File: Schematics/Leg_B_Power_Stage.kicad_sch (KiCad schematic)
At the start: 38 parts, among them Q4 C3M0025065K, Q5 C3M0025065K, U3 UCC21710QDWRQ1, U4 UCC21710QDWRQ1

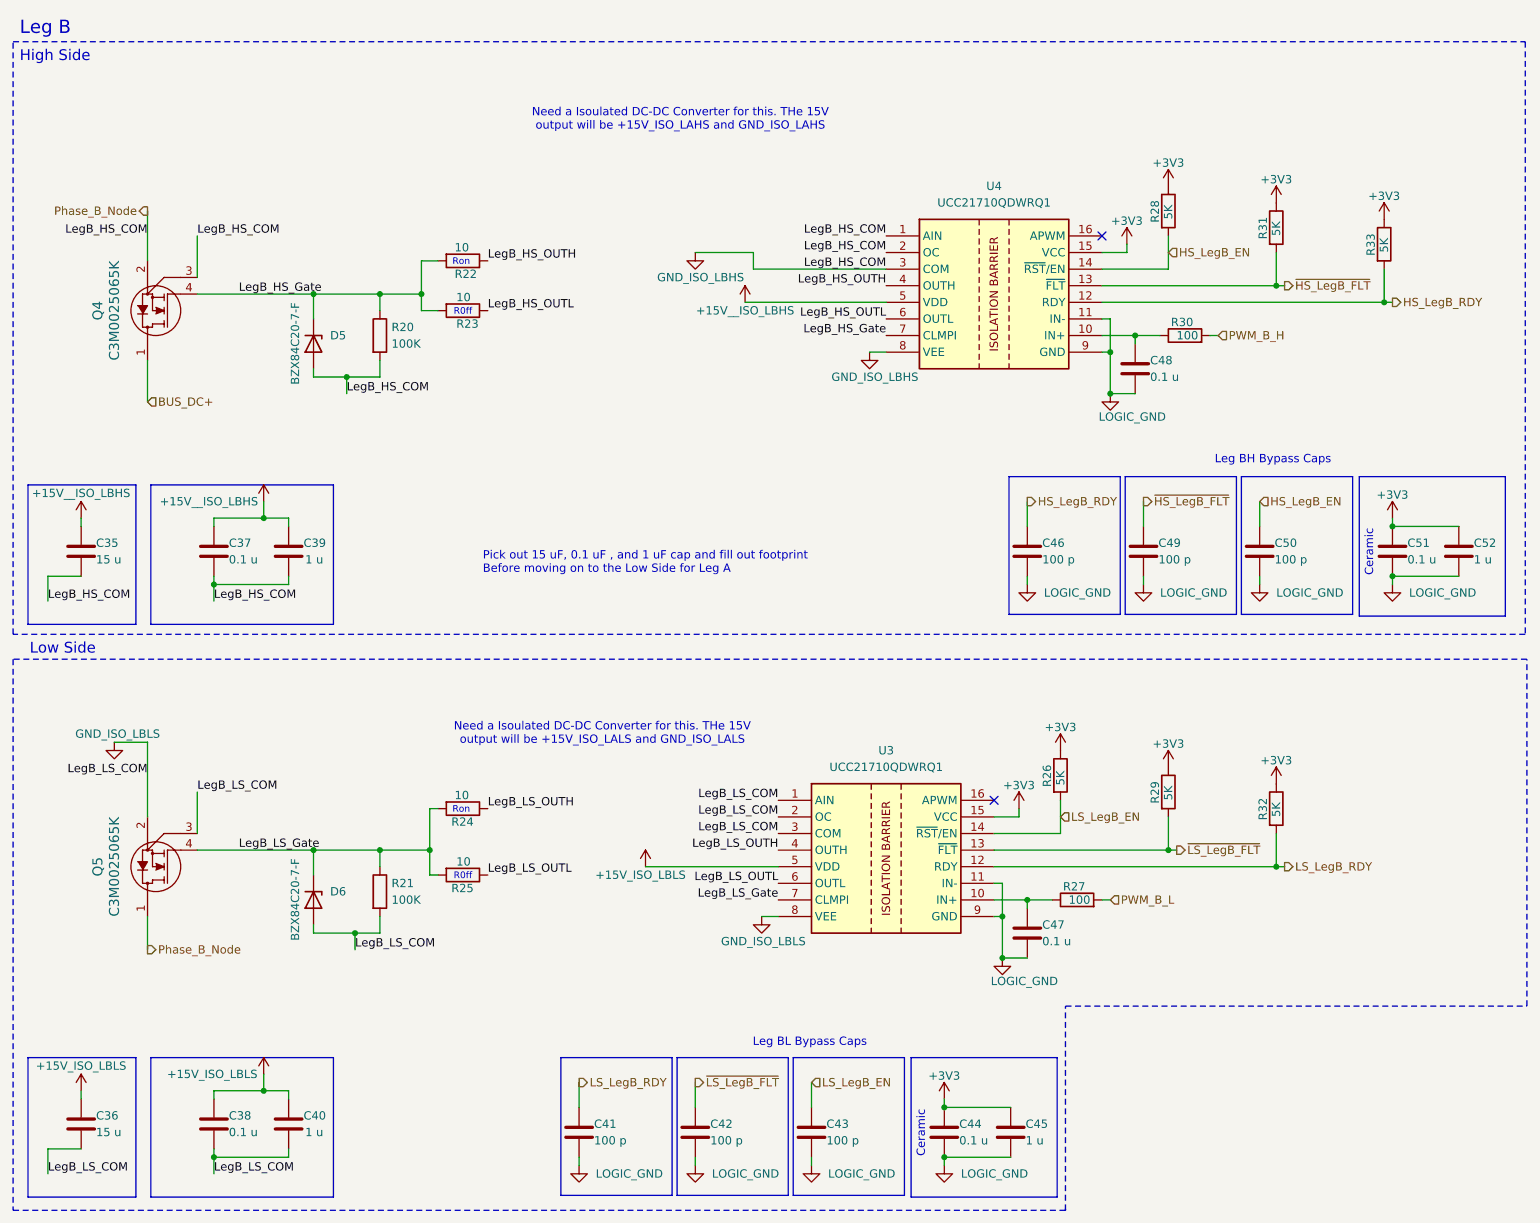
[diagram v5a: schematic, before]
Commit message: [WIP Single Phase SiC Inverter]
- Added molex 4 pin pcb connector for +15V power
- Added 3d model, symbol and footprint
- Added datasheet for molex connector
- Added Male and Female pcb - pcb connectors to all sub sheets
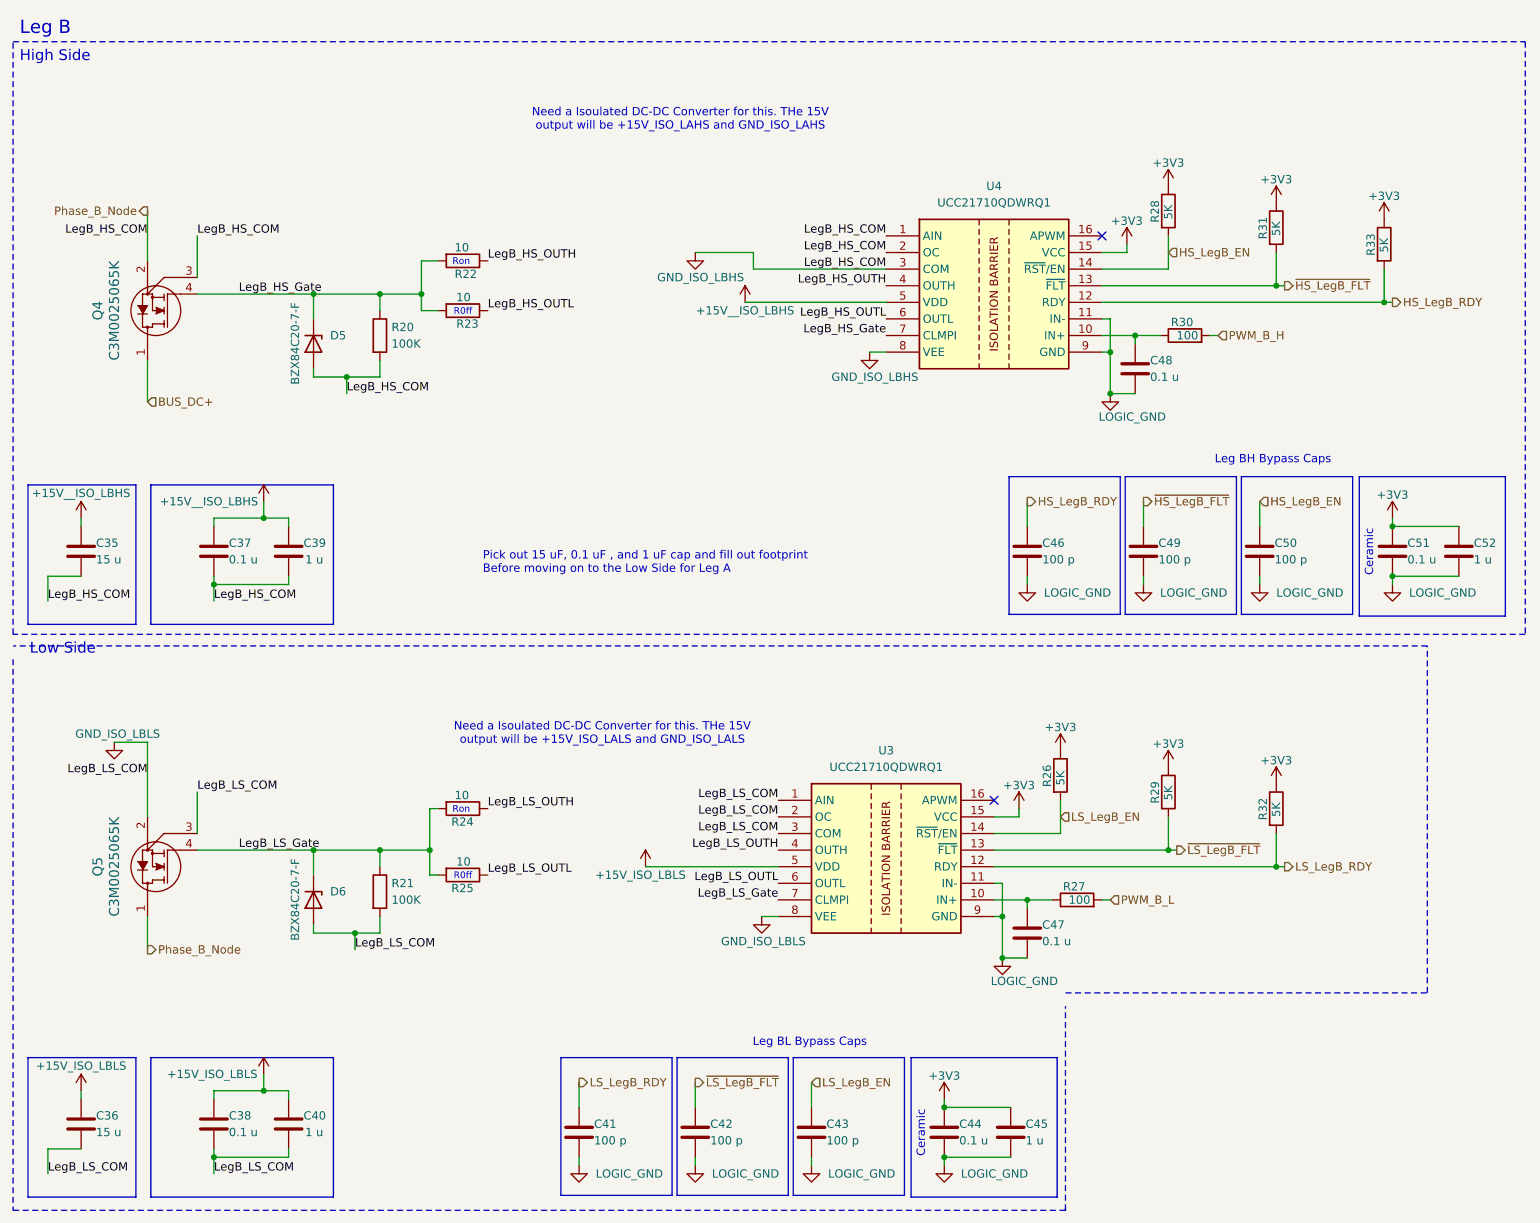
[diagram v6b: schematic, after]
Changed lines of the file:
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@@
 	(polyline
 		(pts
-			(xy 245.364 110.49) (xy 13.716 110.49)
+			(xy 230.124 108.458) (xy 13.716 108.458)
 		)
 		(stroke
@@
 	(polyline
 		(pts
-			(xy 174.752 163.576) (xy 245.364 163.576)
+			(xy 174.752 161.544) (xy 230.124 161.544)
 		)
 		(stroke
@@
 	(polyline
 		(pts
-			(xy 245.364 163.576) (xy 245.364 110.49)
-		)
-		(stroke
+			(xy 230.124 161.544) (xy 230.124 108.458)
+		)
+		(stroke

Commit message: [WIP Single Phase Inverter]
- Changed all Refs within each sub sheet (Stripe)
- Added 3V3 Power Supply off of 15V iso supply
- Added footprint, symbol and 3d part
- updated PCB with new part
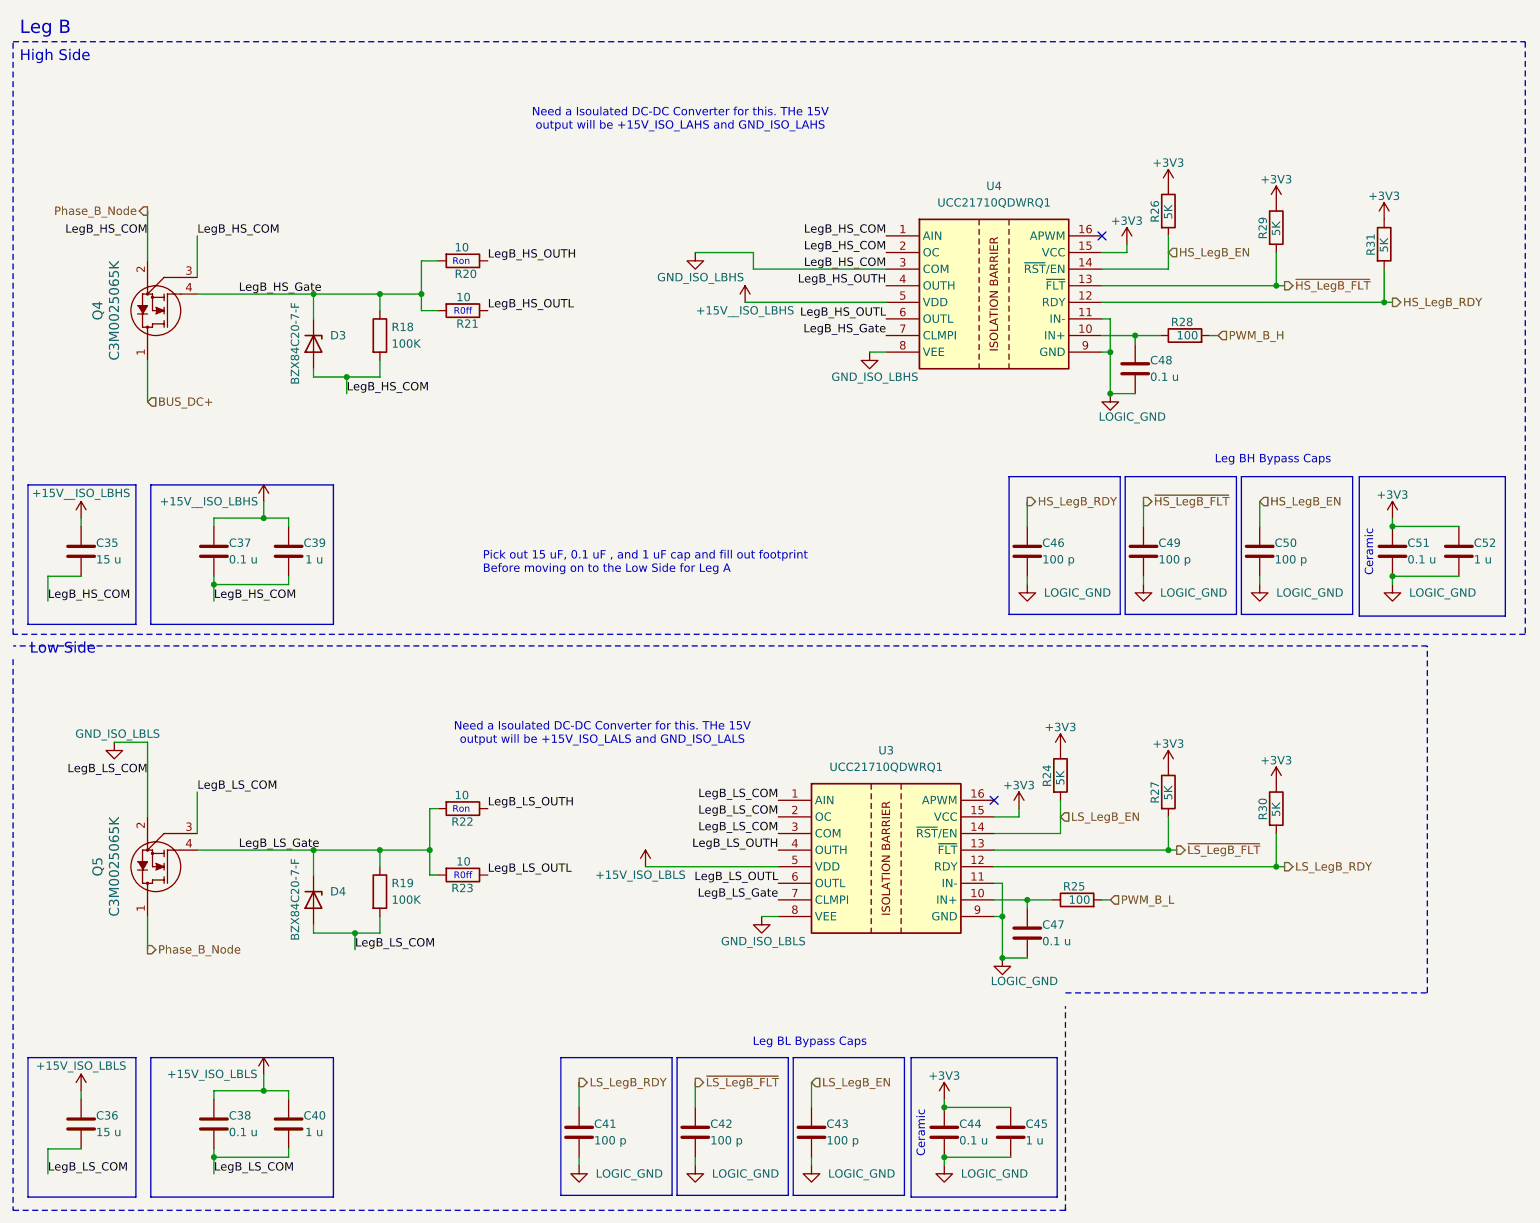
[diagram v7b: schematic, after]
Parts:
- renumbered D5 to D3, D6 to D4, R20 to R18, R21 to R19, R22 to R20, R23 to R21, R24 to R22, R25 to R23, R26 to R24, R27 to R25, R28 to R26, R29 to R27, R30 to R28, R31 to R29, R32 to R30, R33 to R31
